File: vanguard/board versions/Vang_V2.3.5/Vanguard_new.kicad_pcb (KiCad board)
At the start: 4 copper layers, 43.5 x 53.1 mm, 100 parts, among them J1 USB_C_Receptacle_USB2.0_16P, J2 Micro_SD_Card_Det1, J3 Conn_02x03_Odd_Even, J4 Conn_01x03, J5 Conn_01x03, J6 Conn_01x03, J7 Conn_01x02_Pin, Q1 DMG2301L, Q4 BSS138, U1 TPS82130, U10 ATmega4809-A, U12 AP2112K-3.3, U3 ATSAMD11D14A-M, U4 BMP390L, U5 BD1020HFV-TR, U6 AT25DF641A-SH-T, U7 LTC4412xS6, U8 BNO055, U9 TPS61092, Y1 32.768kHz

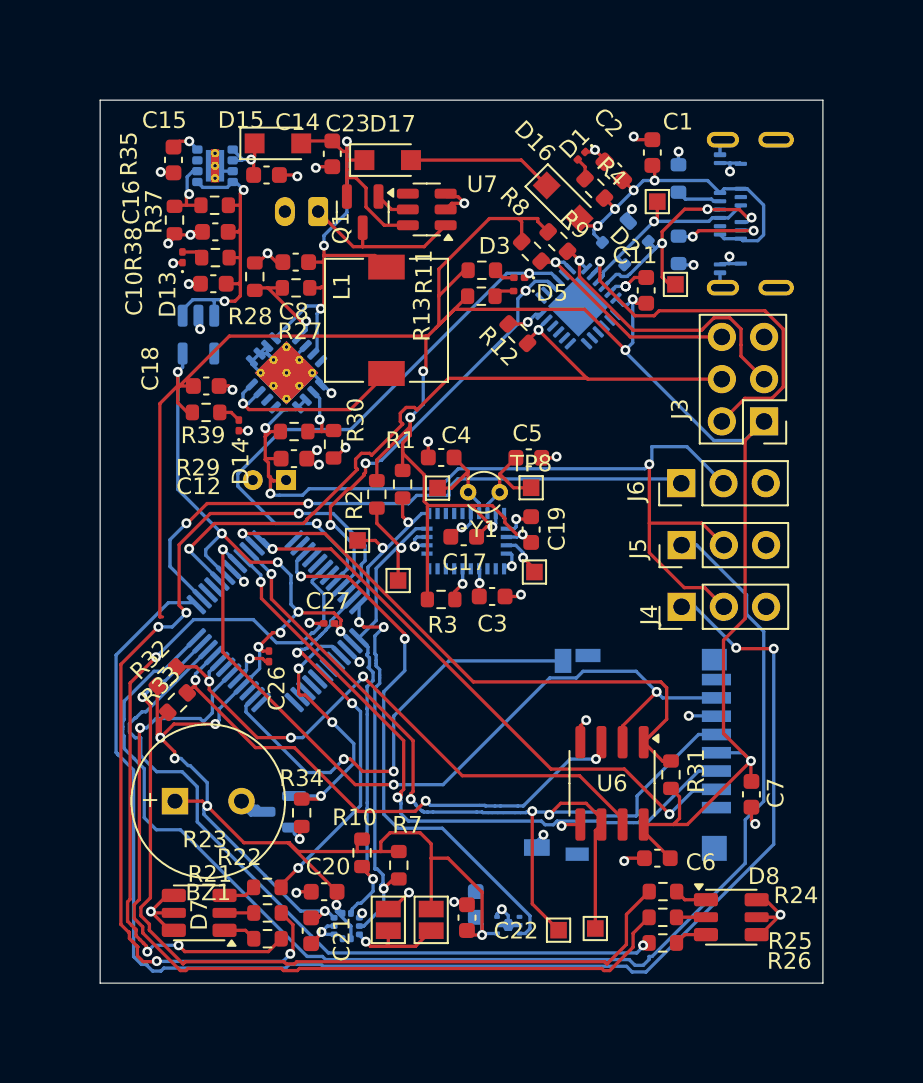
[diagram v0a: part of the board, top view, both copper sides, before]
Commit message: bom + minor fixes
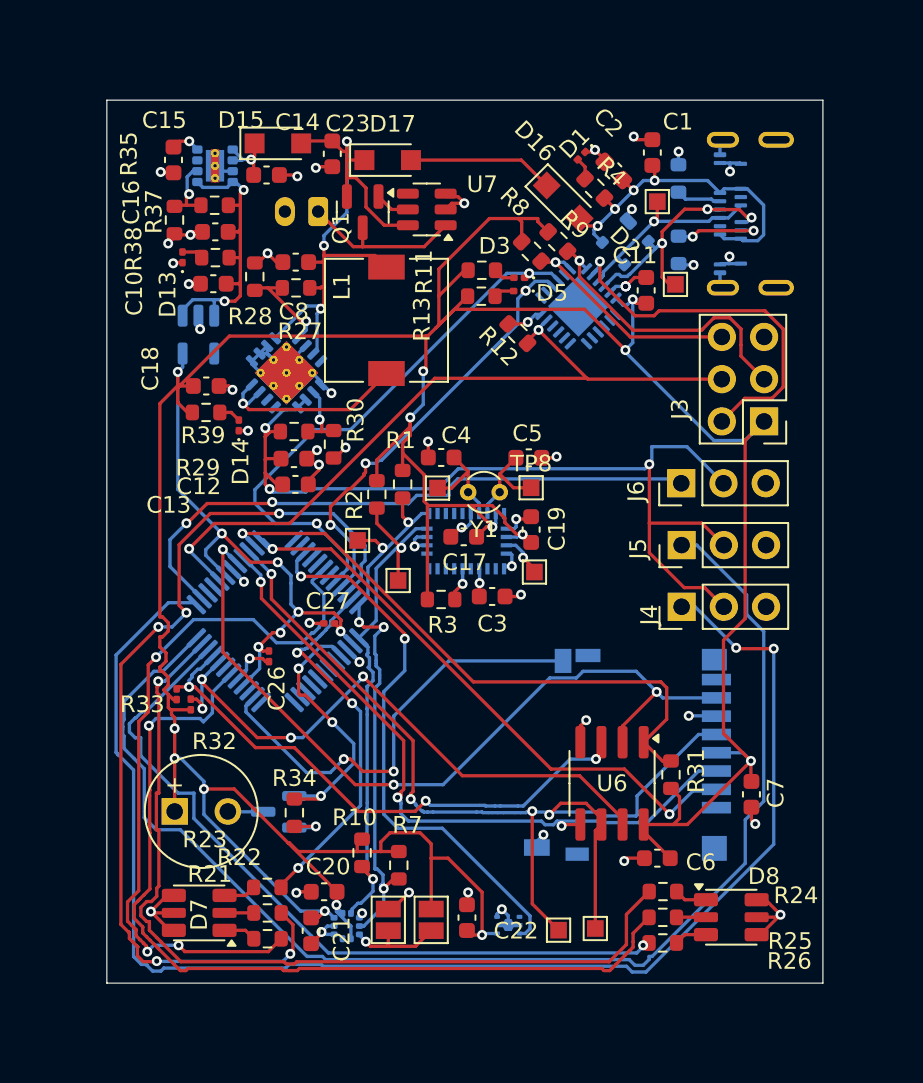
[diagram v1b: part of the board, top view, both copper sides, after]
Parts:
- removed the C22 at (132.2, 124.3)
- BZ1: footprint Buzzer_Beeper:MagneticBuzzer_PUI_AT-0927-TT-6-R -> Buzzer_Beeper:MagneticBuzzer_Kingstate_KCG0601
- C13: footprint Capacitor_THT:CP_Radial_D4.0mm_P2.00mm -> Capacitor_SMD:C_0603_1608Metric; moved to F.Cu
- C17, C19, C20, C21, C26, C27, C3, C6, C7: value 100nF -> 0.1uF
- R32, R33: footprint Resistor_SMD:R_0603_1608Metric -> Resistor_SMD:R_0201_0603Metric
- Y1: value 32.768kHz -> Crystal
- moved R32 2.21 mm to (115.1, 112.3), turned to 90 degrees
- moved C13 0.62 mm to (121.4, 99.1), turned to 0 degrees
- moved BZ1 0.62 mm to (114.1, 118.7)
- moved R33 0.50 mm to (114.2, 111.7), turned to 90 degrees
- moved R34 0.44 mm to (121.3, 118.8)
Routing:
- net TX0: track 35.8 -> 33.8 mm
- net UPDI: track 46.4 -> 45.0 mm
- net Net-(BZ1--): track 3.33 -> 2.13 mm
- net +3.3V: track 263.0 -> 261.8 mm, vias 21 -> 20
- net HOLD: track 35.8 -> 36.7 mm, vias 3 -> 4
- net GND: track 84.8 -> 85.6 mm
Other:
- board size 43.5 x 53.1 mm -> 43.1 x 53.1 mm

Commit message: edits
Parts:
- removed BZ1: Buzzer, Buzzer_Beeper:MagneticBuzzer_Kingstate_KCG0601
- removed C1: 4n7, Capacitor_SMD:C_0603_1608Metric
- removed C10: 1uF, Capacitor_SMD:C_0603_1608Metric
- removed C11: 100nF, Capacitor_SMD:C_0603_1608Metric
- removed C12: 2u2, Capacitor_SMD:C_0603_1608Metric
- removed C13: 100u, Capacitor_SMD:C_0603_1608Metric
- removed C14, C23: 10uF, Capacitor_SMD:C_0603_1608Metric
- removed C15: 3.3 nF, Capacitor_SMD:C_0603_1608Metric
- removed C16: 22uF, Capacitor_SMD:C_0603_1608Metric
- removed C17, C19, C20, C21, C3, C6, C7: 0.1uF, Capacitor_SMD:C_0603_1608Metric
- removed C18: 1u, Capacitor_SMD:C_0603_1608Metric
- removed C2: 100n, Capacitor_SMD:C_0603_1608Metric
- removed C22: C, Capacitor_SMD:C_0603_1608Metric
- removed C26, C27: 0.1uF, Capacitor_SMD:C_0201_0603Metric
- removed C4: 22pF, Capacitor_SMD:C_0603_1608Metric
- removed C5: 22p, Capacitor_SMD:C_0603_1608Metric
- removed C8: 10u, Capacitor_SMD:C_0603_1608Metric
- removed D1, D13, D14, D3, D5: LED, LED_SMD:LED_0201_0603Metric
- removed D15, D16, D17: PMEG6020ER, Diode_SMD:Nexperia_CFP3_SOD-123W
- removed D2: PRTR5V0U2X, Package_TO_SOT_SMD:SOT-143
- removed D7, D8: SMLVN6RGB, LED_SMD:LED_ROHM_SMLVN6
- removed J1: USB_C_Receptacle_USB2.0_16P, Connector_USB:USB_C_Receptacle_Amphenol_124019772112A
- removed J2: Micro_SD_Card_Det1, Connector_Card:microSD_HC_Hirose_DM3D-SF
- removed J3: Conn_02x03_Odd_Even, Connector_PinHeader_2.54mm:PinHeader_2x03_P2.54mm_Vertical
- removed J4, J5, J6: Conn_01x03, Connector_PinHeader_2.54mm:PinHeader_1x03_P2.54mm_Vertical
- removed J7: Conn_01x02_Pin, Connector_JST:JST_PH_B2B-PH-K_1x02_P2.00mm_Vertical
- removed JP1, JP2: Jumper_2_Small_Open, Jumper:SolderJumper-2_P1.3mm_Open_Pad1.0x1.5mm
- removed L1: SLF7055T-6R8N2R8-3PF, Inductor_SMD:L_7.3x7.3_H4.5
- removed Q1: DMG2301L, Package_TO_SOT_SMD:SOT-23
- removed Q4: BSS138, Package_TO_SOT_SMD:SOT-23
- removed R1, R2, R34: 2k2, Resistor_SMD:R_0603_1608Metric
- removed R10, R7, R8, R9: 4k7, Resistor_SMD:R_0603_1608Metric
- removed R11, R13, R39, R4: 330, Resistor_SMD:R_0603_1608Metric
- removed R12: 0, Resistor_SMD:R_0603_1608Metric
- removed R21, R22, R23, R24, R25, R26: 220, Resistor_SMD:R_0603_1608Metric
- removed R27, R28, R30, R37: 100k, Resistor_SMD:R_0603_1608Metric
- removed R29: 315k, Resistor_SMD:R_0603_1608Metric
- removed R3, R31: 10k, Resistor_SMD:R_0603_1608Metric
- removed R32, R33: 10k, Resistor_SMD:R_0201_0603Metric
- removed R35: 350k, Resistor_SMD:R_0603_1608Metric
- removed R38: 100, Resistor_SMD:R_0603_1608Metric
- removed R5, R6: 5k1, Resistor_SMD:R_0603_1608Metric
- removed TP1, TP2, TP3, TP4, TP5, TP6, TP7, TP8, TP9: TestPoint, TestPoint:TestPoint_Pad_1.0x1.0mm
- removed U1: TPS82130, Package_LGA:Texas_SIL0008D_MicroSiP-8-1EP_2.8x3mm_P0.65mm_EP1.1x1.9mm_ThermalVias
- removed U10: ATmega4809-A, Package_QFP:TQFP-48_7x7mm_P0.5mm
- removed U12: AP2112K-3.3, Package_TO_SOT_SMD:SOT-23-5
- removed U3: ATSAMD11D14A-M, Package_DFN_QFN:QFN-24-1EP_4x4mm_P0.5mm_EP2.6x2.6mm
- removed U4: BMP390L, Package_LGA:ST_HLGA-10_2x2mm_P0.5mm_LayoutBorder3x2y
- removed U5: BD1020HFV-TR, Package_TO_SOT_SMD:HVSOF5
- removed U6: AT25DF641A-SH-T, Package_SO:SOIC-8_3.9x4.9mm_P1.27mm
- removed U7: LTC4412xS6, Package_TO_SOT_SMD:TSOT-23-6
- removed U8: BNO055, Package_LGA:LGA-28_5.2x3.8mm_P0.5mm
- removed U9: TPS61092, Package_DFN_QFN:Texas_RSA_VQFN-16-1EP_4x4mm_P0.65mm_EP2.7x2.7mm_ThermalVias
- removed Y1: Crystal, Crystal:Crystal_C26-LF_D2.1mm_L6.5mm_Vertical
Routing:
- net +3.3V: track 261.8 -> 0.00 mm, vias 20 -> 0
- net PORT_SERVO: track 85.6 -> 0.00 mm, vias 2 -> 0
- net GND: track 85.6 -> 0.00 mm, vias 50 -> 0
- net STAR_SERVO: track 78.1 -> 0.00 mm
- net SCK: track 59.1 -> 0.00 mm, vias 4 -> 0
- net +5V: track 57.2 -> 0.00 mm, vias 3 -> 0
- net STAR_RED: track 56.0 -> 0.00 mm, vias 5 -> 0
- net PORT_RED: track 53.8 -> 0.00 mm, vias 1 -> 0
- net PORT_BLUE: track 53.6 -> 0.00 mm, vias 1 -> 0
- net MISO: track 47.8 -> 0.00 mm, vias 3 -> 0
- net PORT_GREEN: track 45.7 -> 0.00 mm, vias 1 -> 0
- net UPDI: track 45.0 -> 0.00 mm, vias 2 -> 0
- net STAR_BLUE: track 43.5 -> 0.00 mm, vias 3 -> 0
- net MOSI: track 41.5 -> 0.00 mm, vias 3 -> 0
- net EJEC_SERVO: track 37.1 -> 0.00 mm, vias 2 -> 0
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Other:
- board size 43.1 x 53.1 mm -> 43.5 x 53.1 mm
